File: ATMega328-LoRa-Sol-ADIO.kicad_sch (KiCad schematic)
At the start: 48 parts, among them J1 USB_B_Micro, J2 External Power, J3 AIO/I2C, J4 Solar, J5 RXTX+Power, J6 SMA, J7 Conn_01x06, Q1 IRLML5203, U1 AP1117-33, U2 CH340G, U3 LP2985-3.3, U4 RFM95W-868S2, U5 SPV1040TTR, U6 ATmega328P-A, U7 DS3231M, Y1 12MHz, Y2 8MHz

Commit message: Further work on the ATMega328 PCB
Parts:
- BT1: footprint Battery:BatteryHolder_Keystone_1042_1x18650 -> Battery:BatteryHolder_MPD_BH-18650-PC2
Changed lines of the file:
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@@
       (effects (font (size 1.27 1.27)) (justify left))
     )
-    (property "Footprint" "Battery:BatteryHolder_Keystone_1042_1x18650" (id 2) (at 163.83 182.626 90)
+    (property "Footprint" "Battery:BatteryHolder_MPD_BH-18650-PC2" (id 2) (at 163.83 182.626 90)
       (effects (font (size 1.27 1.27)) hide)
     )
@@
     )
     (path "/c5a88760-ec4e-4d44-9244-a0070f391982"
-      (reference "BT1") (unit 1) (value "18650") (footprint "Battery:BatteryHolder_Keystone_1042_1x18650")
+      (reference "BT1") (unit 1) (value "18650") (footprint "Battery:BatteryHolder_MPD_BH-18650-PC2")
     )
     (path "/150e8d39-fc96-4381-ab55-5b22188e2083"

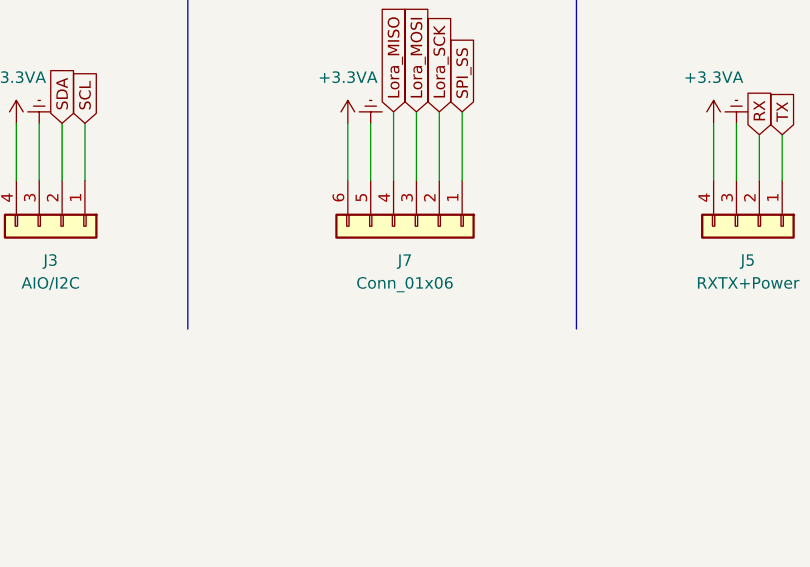
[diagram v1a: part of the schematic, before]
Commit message: Update the PCB Board and add nets to it
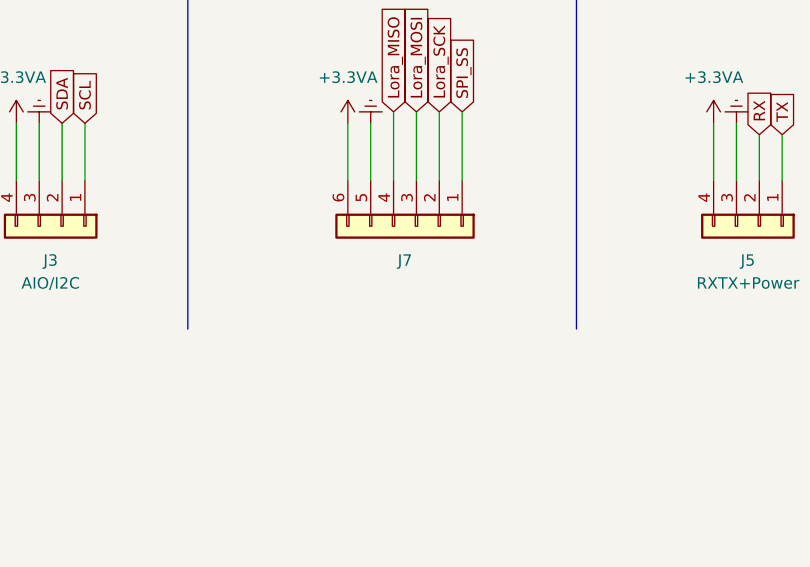
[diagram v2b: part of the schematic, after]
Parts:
- J7: value Conn_01x06 -> (none)
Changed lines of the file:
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@@
   )
   (symbol (lib_id "Connector_Generic:Conn_01x06") (at 233.68 153.67 270) (unit 1)
-    (in_bom yes) (on_board yes) (fields_autoplaced)
+    (in_bom yes) (on_board yes)
     (property "Reference" "J7" (id 0) (at 232.41 157.48 90))
-    (property "Value" "Conn_01x06" (id 1) (at 232.41 160.02 90))
+    (property "Value" "" (id 1) (at 229.87 160.02 90))
     (property "Footprint" "Connector_JST:JST_XH_B6B-XH-A_1x06_P2.50mm_Vertical" (id 2) (at 233.68 153.67 0)
       (effects (font (size 1.27 1.27)) hide)
@@
     )
     (path "/708f0346-bb99-4055-ad19-07185a4fa006"
-      (reference "J7") (unit 1) (value "Conn_01x06") (footprint "Connector_JST:JST_XH_B6B-XH-A_1x06_P2.50mm_Vertical")
+      (reference "J7") (unit 1) (value "SPI") (footprint "Connector_JST:JST_XH_B6B-XH-A_1x06_P2.50mm_Vertical")
     )
     (path "/37945251-8e34-4d85-9e9d-82a9160102c8"

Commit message: First set of gerber files for production
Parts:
- added D4: B5817WS-TP, Diode_SMD:D_SOD-323_HandSoldering, symbol Device:D_Schottky_Filled
- added JP2: Solar Powered, Jumper:SolderJumper-2_P1.3mm_Open_Pad1.0x1.5mm, symbol Jumper:SolderJumper_2_Open
- J7: value (none) -> SPI
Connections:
- net +BATT: now also D4.1 (K), JP2.2 (B); no longer BT1.1 (+)
- new net: BT1.1 (+), D4.2 (A), JP2.1 (A)
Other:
- note added: "Battery"
- note added: "Solar Connector"
- note added: "Solar Loading IC"
- note added: "The PCB can be used Solar Powered or just with a 18650 LiPo Battery which can be loaded externally - for Solar Powered connect JP2 otherwise add a Schottky Diode to D4. The CR2032 can be replaced by connecting JP1 and using the 18650 as backup battery for the clock"
- moved on the sheet: BT1
